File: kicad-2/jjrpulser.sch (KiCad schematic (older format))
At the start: 20 parts, among them J1 USB_OTG, J3 Screw_Terminal_HOT, J4 Screw_Terminal_COLD, J5 Conn_UART, U1 ESP-12, U2 NCP1117-3.3_SOT223

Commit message: Разводка в процессе
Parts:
- removed J1: USB_OTG, Connectors:USB_Micro-B, symbol USB_OTG
- C1: value 100mkF -> 10mkF 16v
- C2: value 470mkF -> 22mkF 5v
- U2: value NCP1117-3.3_SOT223 -> AMS1117-3.3_SOT223
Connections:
- no-connect marks 9 -> 5
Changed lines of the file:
@@
 LIBS:valves
 LIBS:ESP8266
+LIBS:jjrpulser-cache
 EELAYER 25 0
 EELAYER END
@@
 P 3450 3600
 F 0 "#FLG013" H 3450 3675 50  0001 C CNN
-F 1 "PWR_FLAG" H 3450 3750 50  0000 C CNN
+F 1 "PWR_FLAG" V 3450 3750 50  0000 L CNN
 F 2 "" H 3450 3600 50  0001 C CNN
 F 3 "" H 3450 3600 50  0001 C CNN
@@
 P 2750 3600
 F 0 "U2" H 2600 3725 50  0000 C CNN
-F 1 "NCP1117-3.3_SOT223" H 2750 3725 50  0000 L CNN
+F 1 "AMS1117-3.3_SOT223" V 2750 3725 50  0000 L CNN
 F 2 "TO_SOT_Packages_SMD:SOT-223-3Lead_TabPin2" H 2750 3800 50  0001 C CNN
 F 3 "" H 2850 3350 50  0001 C CNN
 	1    2750 3600
-	1    0    0    -1
-$EndComp
-$Comp
-L USB_OTG J1
-U 1 1 5D018B49
-P 1800 3800
-F 0 "J1" H 1600 4250 50  0000 L CNN
-F 1 "USB_OTG" H 1600 4150 50  0000 L CNN
-F 2 "Connectors:USB_Micro-B" H 1950 3750 50  0001 C CNN
-F 3 "" H 1950 3750 50  0001 C CNN
-	1    1800 3800
 	1    0    0    -1
 $EndComp
@@
 P 2300 3750
 F 0 "C1" H 2325 3850 50  0000 L CNN
-F 1 "100mkF" H 2325 3650 50  0000 L CNN
+F 1 "10mkF 16v" V 2325 3650 50  0000 R CNN
 F 2 "Capacitors_SMD:CP_Elec_6.3x5.3" H 2338 3600 50  0001 C CNN
 F 3 "" H 2300 3750 50  0001 C CNN
@@
 P 3200 3750
 F 0 "C2" H 3225 3850 50  0000 L CNN
-F 1 "470mkF" H 3225 3650 50  0000 L CNN
+F 1 "22mkF 5v" V 3225 3650 50  0000 R CNN
 F 2 "Capacitors_SMD:CP_Elec_6.3x5.3" H 3238 3600 50  0001 C CNN
 F 3 "" H 3200 3750 50  0001 C CNN
@@
 	1    0    0    -1
 $EndComp
-NoConn ~ 1700 4200
-NoConn ~ 2100 3800
-NoConn ~ 2100 3900
-NoConn ~ 2100 4000
 $Comp
 L Earth #PWR021
@@
 P 2100 3600
 F 0 "#FLG022" H 2100 3675 50  0001 C CNN
-F 1 "PWR_FLAG" H 2100 3750 50  0000 C CNN
+F 1 "PWR_FLAG" V 2100 3750 50  0000 L CNN
 F 2 "" H 2100 3600 50  0001 C CNN
 F 3 "" H 2100 3600 50  0001 C CNN

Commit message: Новая разводка: замена micro-USB на обычный разъем питания
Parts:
- added J1: Conn_Coaxial_Power, Connectors_TE-Connectivity:BNC_Socket_TYCO-AMP_LargePads, symbol Conn_Coaxial_Power
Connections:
- net +5V: now also C1.1, U2.3 (VI), J1.1 (In)
- net Earth: now also J1.2 (Ext)
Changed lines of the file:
@@
 $EndComp
 Wire Wire Line
-	2100 3600 2450 3600
+	1800 3600 2450 3600
 $Comp
 L CP C1
@@
 L Earth #PWR018
 U 1 1 5D018FC9
-P 1800 4200
-F 0 "#PWR018" H 1800 3950 50  0001 C CNN
-F 1 "Earth" H 1800 4050 50  0001 C CNN
-F 2 "" H 1800 4200 50  0001 C CNN
-F 3 "" H 1800 4200 50  0001 C CNN
-	1    1800 4200
+P 1800 3900
+F 0 "#PWR018" H 1800 3650 50  0001 C CNN
+F 1 "Earth" H 1800 3750 50  0001 C CNN
+F 2 "" H 1800 3900 50  0001 C CNN
+F 3 "" H 1800 3900 50  0001 C CNN
+	1    1800 3900
 	1    0    0    -1
 $EndComp
@@
 	1    0    0    -1
 $EndComp
+$Comp
+L Conn_Coaxial_Power J1
+U 1 1 5D07B797
+P 1800 3700
+F 0 "J1" V 1600 3650 50  0000 C CNN
+F 1 "Conn_Coaxial_Power" V 1675 3650 50  0000 C CNN
+F 2 "Connectors_TE-Connectivity:BNC_Socket_TYCO-AMP_LargePads" H 1800 3650 50  0001 C CNN
+F 3 "" H 1800 3650 50  0001 C CNN
+	1    1800 3700
+	1    0    0    -1
+$EndComp
+$Comp
+L +5V #PWR023
+U 1 1 5D07B846
+P 1800 3600
+F 0 "#PWR023" H 1800 3450 50  0001 C CNN
+F 1 "+5V" H 1800 3740 50  0000 C CNN
+F 2 "" H 1800 3600 50  0001 C CNN
+F 3 "" H 1800 3600 50  0001 C CNN
+	1    1800 3600
+	1    0    0    -1
+$EndComp
+Connection ~ 2100 3600
 $EndSCHEMATC

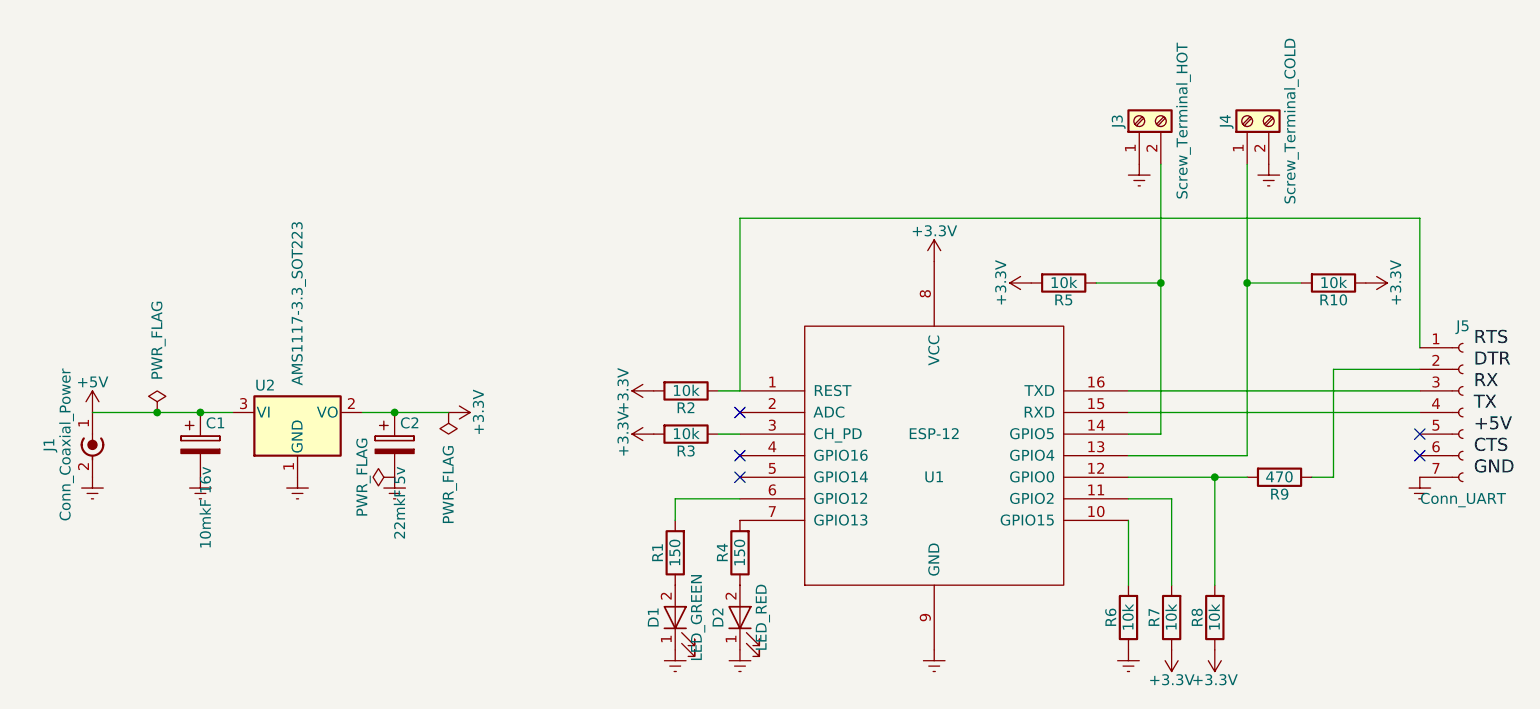
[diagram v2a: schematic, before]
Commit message: Разводка2: +5V с UART - программирование и консоль без внешнего питания. GPIO16 <--> RESET - выход из deep sleep
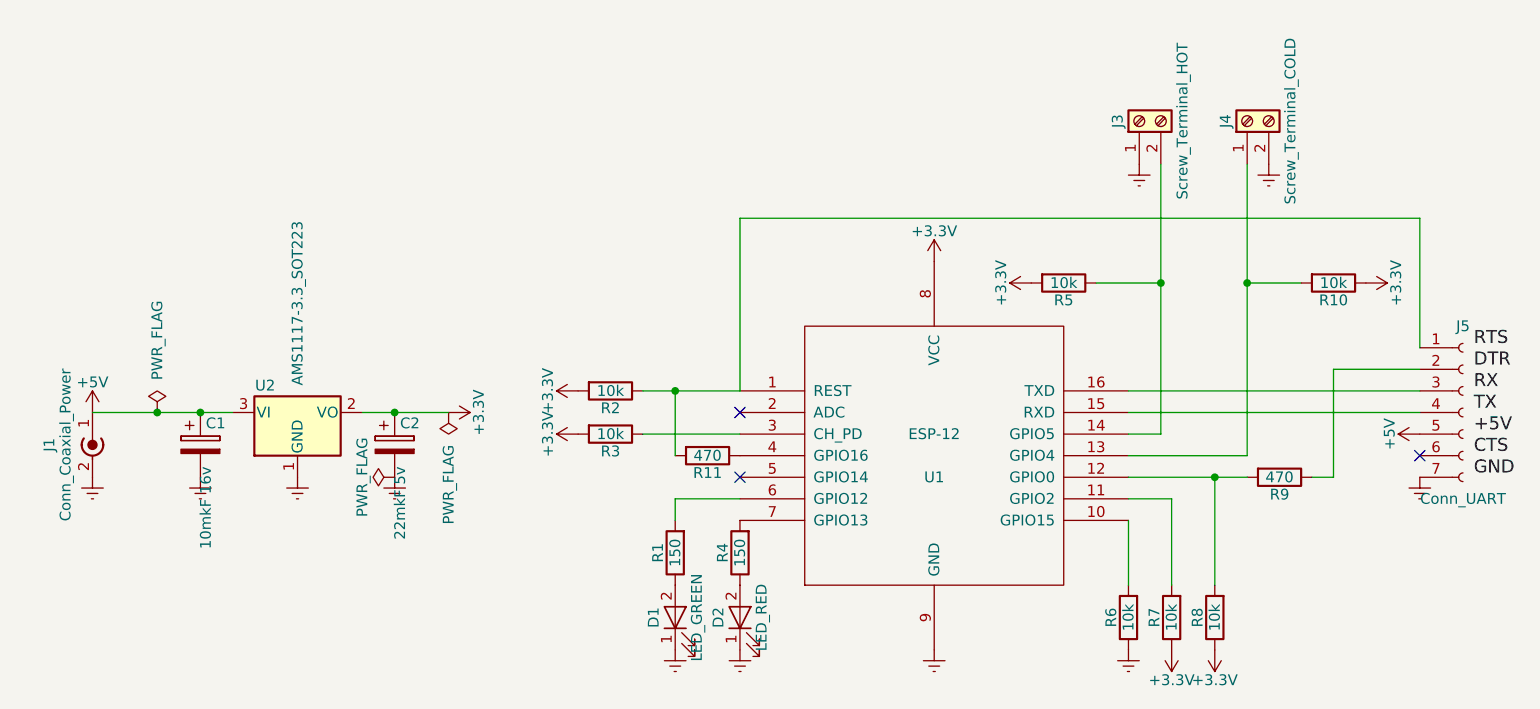
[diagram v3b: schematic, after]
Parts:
- added R11: 470, Resistors_SMD:R_0805_HandSoldering, symbol R
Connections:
- net +5V: now also J5.5 (Pin_5)
- net at J5.1 (Pin_1), R2.1, U1.1 (REST): now also R11.2
- net at U1.4 (GPIO16): now also R11.1
- no-connect marks 5 -> 3
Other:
- moved on the sheet: R2, R3
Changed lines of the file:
@@
 L R R2
 U 1 1 5C352E95
-P 4550 3500
-F 0 "R2" V 4630 3500 50  0000 C CNN
-F 1 "10k" V 4550 3500 50  0000 C CNN
-F 2 "Resistors_SMD:R_0805_HandSoldering" V 4480 3500 50  0001 C CNN
-F 3 "" H 4550 3500 50  0001 C CNN
-	1    4550 3500
+P 4200 3500
+F 0 "R2" V 4280 3500 50  0000 C CNN
+F 1 "10k" V 4200 3500 50  0000 C CNN
+F 2 "Resistors_SMD:R_0805_HandSoldering" V 4130 3500 50  0001 C CNN
+F 3 "" H 4200 3500 50  0001 C CNN
+	1    4200 3500
 	0    1    1    0
 $EndComp
@@
 L R R3
 U 1 1 5C35306E
-P 4550 3700
-F 0 "R3" V 4630 3700 50  0000 C CNN
-F 1 "10k" V 4550 3700 50  0000 C CNN
-F 2 "Resistors_SMD:R_0805_HandSoldering" V 4480 3700 50  0001 C CNN
-F 3 "" H 4550 3700 50  0001 C CNN
-	1    4550 3700
+P 4200 3700
+F 0 "R3" V 4280 3700 50  0000 C CNN
+F 1 "10k" V 4200 3700 50  0000 C CNN
+F 2 "Resistors_SMD:R_0805_HandSoldering" V 4130 3700 50  0001 C CNN
+F 3 "" H 4200 3700 50  0001 C CNN
+	1    4200 3700
 	0    1    1    0
 $EndComp
@@
 $EndComp
 $Comp
-L +3.3V #PWR01
+L +3.3V #PWR11
 U 1 1 5C353620
 P 5700 2900
-F 0 "#PWR01" H 5700 2750 50  0001 C CNN
+F 0 "#PWR11" H 5700 2750 50  0001 C CNN
 F 1 "+3.3V" H 5700 3040 50  0000 C CNN
 F 2 "" H 5700 2900 50  0001 C CNN
@@
 $EndComp
 $Comp
-L Earth #PWR02
+L Earth #PWR12
 U 1 1 5C35375C
 P 5700 4700
-F 0 "#PWR02" H 5700 4450 50  0001 C CNN
+F 0 "#PWR12" H 5700 4450 50  0001 C CNN
 F 1 "Earth" H 5700 4550 50  0001 C CNN
 F 2 "" H 5700 4700 50  0001 C CNN
@@
 $EndComp
 $Comp
-L Earth #PWR03
+L Earth #PWR14
 U 1 1 5C3547A3
 P 6600 4700
-F 0 "#PWR03" H 6600 4450 50  0001 C CNN
+F 0 "#PWR14" H 6600 4450 50  0001 C CNN
 F 1 "Earth" H 6600 4550 50  0001 C CNN
 F 2 "" H 6600 4700 50  0001 C CNN
@@
 GND
 $Comp
-L +3.3V #PWR04
+L +3.3V #PWR19
 U 1 1 5C35542B
 P 7700 3000
-F 0 "#PWR04" H 7700 2850 50  0001 C CNN
+F 0 "#PWR19" H 7700 2850 50  0001 C CNN
 F 1 "+3.3V" H 7700 3140 50  0000 C CNN
 F 2 "" H 7700 3000 50  0001 C CNN
@@
 $EndComp
 $Comp
-L +3.3V #PWR05
+L +3.3V #PWR17
 U 1 1 5C3554B7
 P 7000 4700
-F 0 "#PWR05" H 7000 4550 50  0001 C CNN
+F 0 "#PWR17" H 7000 4550 50  0001 C CNN
 F 1 "+3.3V" H 7000 4840 50  0000 C CNN
 F 2 "" H 7000 4700 50  0001 C CNN
@@
 $EndComp
 $Comp
-L +3.3V #PWR06
+L +3.3V #PWR16
 U 1 1 5C3554EC
 P 6800 4700
-F 0 "#PWR06" H 6800 4550 50  0001 C CNN
+F 0 "#PWR16" H 6800 4550 50  0001 C CNN
 F 1 "+3.3V" H 6800 4840 50  0000 C CNN
 F 2 "" H 6800 4700 50  0001 C CNN
@@
 $EndComp
 $Comp
-L Earth #PWR07
+L Earth #PWR21
 U 1 1 5C3555CB
 P 7950 3900
-F 0 "#PWR07" H 7950 3650 50  0001 C CNN
+F 0 "#PWR21" H 7950 3650 50  0001 C CNN
 F 1 "Earth" H 7950 3750 50  0001 C CNN
 F 2 "" H 7950 3900 50  0001 C CNN
@@
 $EndComp
 $Comp
-L +3.3V #PWR08
+L +3.3V #PWR13
 U 1 1 5C355706
 P 6150 3000
-F 0 "#PWR08" H 6150 2850 50  0001 C CNN
+F 0 "#PWR13" H 6150 2850 50  0001 C CNN
 F 1 "+3.3V" H 6150 3140 50  0000 C CNN
 F 2 "" H 6150 3000 50  0001 C CNN
@@
 $EndComp
 $Comp
-L Earth #PWR09
+L Earth #PWR9
 U 1 1 5C35594F
 P 4500 4700
-F 0 "#PWR09" H 4500 4450 50  0001 C CNN
+F 0 "#PWR9" H 4500 4450 50  0001 C CNN
 F 1 "Earth" H 4500 4550 50  0001 C CNN
 F 2 "" H 4500 4700 50  0001 C CNN
@@
 $EndComp
 $Comp
-L Earth #PWR010
+L Earth #PWR10
 U 1 1 5C3559DA
 P 4800 4700
-F 0 "#PWR010" H 4800 4450 50  0001 C CNN
+F 0 "#PWR10" H 4800 4450 50  0001 C CNN
 F 1 "Earth" H 4800 4550 50  0001 C CNN
 F 2 "" H 4800 4700 50  0001 C CNN
@@
 $EndComp
 NoConn ~ 4800 3900
-NoConn ~ 4800 3800
-NoConn ~ 7950 3700
 NoConn ~ 7950 3800
 NoConn ~ 4800 3600
 $Comp
-L +3.3V #PWR011
+L +3.3V #PWR7
 U 1 1 5C355B7E
-P 4400 3500
-F 0 "#PWR011" H 4400 3350 50  0001 C CNN
-F 1 "+3.3V" H 4400 3640 50  0000 C CNN
-F 2 "" H 4400 3500 50  0001 C CNN
-F 3 "" H 4400 3500 50  0001 C CNN
-	1    4400 3500
-	0    -1   -1   0
-$EndComp
-$Comp
-L +3.3V #PWR012
+P 4050 3500
+F 0 "#PWR7" H 4050 3350 50  0001 C CNN
+F 1 "+3.3V" H 4050 3640 50  0000 C CNN
+F 2 "" H 4050 3500 50  0001 C CNN
+F 3 "" H 4050 3500 50  0001 C CNN
+	1    4050 3500
+	0    -1   -1   0
+$EndComp
+$Comp
+L +3.3V #PWR8
 U 1 1 5C355C5B
-P 4400 3700
-F 0 "#PWR012" H 4400 3550 50  0001 C CNN
-F 1 "+3.3V" H 4400 3840 50  0000 C CNN
-F 2 "" H 4400 3700 50  0001 C CNN
-F 3 "" H 4400 3700 50  0001 C CNN
-	1    4400 3700
-	0    -1   -1   0
-$EndComp
-$Comp
-L PWR_FLAG #FLG013
+P 4050 3700
+F 0 "#PWR8" H 4050 3550 50  0001 C CNN
+F 1 "+3.3V" H 4050 3840 50  0000 C CNN
+F 2 "" H 4050 3700 50  0001 C CNN
+F 3 "" H 4050 3700 50  0001 C CNN
+	1    4050 3700
+	0    -1   -1   0
+$EndComp
+$Comp
+L PWR_FLAG #FLG3
 U 1 1 5C356F0A
 P 3450 3600
-F 0 "#FLG013" H 3450 3675 50  0001 C CNN
+F 0 "#FLG3" H 3450 3675 50  0001 C CNN
 F 1 "PWR_FLAG" V 3450 3750 50  0000 L CNN
 F 2 "" H 3450 3600 50  0001 C CNN
@@
 $EndComp
 $Comp
-L +3.3V #PWR014
+L +3.3V #PWR6
 U 1 1 5C359F14
 P 3450 3600
-F 0 "#PWR014" H 3450 3450 50  0001 C CNN
+F 0 "#PWR6" H 3450 3450 50  0001 C CNN
 F 1 "+3.3V" H 3450 3740 50  0000 C CNN
 F 2 "" H 3450 3600 50  0001 C CNN
@@
 $EndComp
 $Comp
-L Earth #PWR015
+L Earth #PWR18
 U 1 1 5CBC9513
 P 7250 2450
-F 0 "#PWR015" H 7250 2200 50  0001 C CNN
+F 0 "#PWR18" H 7250 2200 50  0001 C CNN
 F 1 "Earth" H 7250 2300 50  0001 C CNN
 F 2 "" H 7250 2450 50  0001 C CNN
@@
 $EndComp
 $Comp
-L Earth #PWR016
+L Earth #PWR15
 U 1 1 5CBC956E
 P 6650 2450
-F 0 "#PWR016" H 6650 2200 50  0001 C CNN
+F 0 "#PWR15" H 6650 2200 50  0001 C CNN
 F 1 "Earth" H 6650 2300 50  0001 C CNN
 F 2 "" H 6650 2450 50  0001 C CNN
@@
 	6600 3500 7950 3500
 Wire Wire Line
-	4700 3700 4800 3700
-Wire Wire Line
-	4700 3500 4800 3500
+	4350 3700 4800 3700
+Wire Wire Line
+	4350 3500 4800 3500
 Wire Wire Line
 	4800 3500 4800 2700
@@
 	6600 3900 7150 3900
 $Comp
-L PWR_FLAG #FLG017
+L PWR_FLAG #FLG2
 U 1 1 5CBE1549
 P 3200 3900
-F 0 "#FLG017" H 3200 3975 50  0001 C CNN
+F 0 "#FLG2" H 3200 3975 50  0001 C CNN
 F 1 "PWR_FLAG" H 3200 4050 50  0000 C CNN
 F 2 "" H 3200 3900 50  0001 C CNN
@@
 $EndComp
 $Comp
-L Earth #PWR018
+L Earth #PWR2
 U 1 1 5D018FC9
 P 1800 3900
-F 0 "#PWR018" H 1800 3650 50  0001 C CNN
+F 0 "#PWR2" H 1800 3650 50  0001 C CNN
 F 1 "Earth" H 1800 3750 50  0001 C CNN
 F 2 "" H 1800 3900 50  0001 C CNN
@@
 $EndComp
 $Comp
-L Earth #PWR019
+L Earth #PWR3
 U 1 1 5D0190D4
 P 2300 3900
-F 0 "#PWR019" H 2300 3650 50  0001 C CNN
+F 0 "#PWR3" H 2300 3650 50  0001 C CNN
 F 1 "Earth" H 2300 3750 50  0001 C CNN
 F 2 "" H 2300 3900 50  0001 C CNN
@@
 Connection ~ 3200 3600
 $Comp
-L Earth #PWR020
+L Earth #PWR5
 U 1 1 5D019215
 P 3200 3900
-F 0 "#PWR020" H 3200 3650 50  0001 C CNN
+F 0 "#PWR5" H 3200 3650 50  0001 C CNN
 F 1 "Earth" H 3200 3750 50  0001 C CNN
 F 2 "" H 3200 3900 50  0001 C CNN
@@
 $EndComp
 $Comp
-L Earth #PWR021
+L Earth #PWR4
 U 1 1 5D019E44
 P 2750 3900
-F 0 "#PWR021" H 2750 3650 50  0001 C CNN
+F 0 "#PWR4" H 2750 3650 50  0001 C CNN
 F 1 "Earth" H 2750 3750 50  0001 C CNN
 F 2 "" H 2750 3900 50  0001 C CNN
@@
 $EndComp
 $Comp
-L PWR_FLAG #FLG022
+L PWR_FLAG #FLG1
 U 1 1 5D01A028
 P 2100 3600
-F 0 "#FLG022" H 2100 3675 50  0001 C CNN
+F 0 "#FLG1" H 2100 3675 50  0001 C CNN
 F 1 "PWR_FLAG" V 2100 3750 50  0000 L CNN
 F 2 "" H 2100 3600 50  0001 C CNN
@@
 $EndComp
 $Comp
-L +5V #PWR023
+L +5V #PWR1
 U 1 1 5D07B846
 P 1800 3600
-F 0 "#PWR023" H 1800 3450 50  0001 C CNN
+F 0 "#PWR1" H 1800 3450 50  0001 C CNN
 F 1 "+5V" H 1800 3740 50  0000 C CNN
 F 2 "" H 1800 3600 50  0001 C CNN
@@
 $EndComp
 Connection ~ 2100 3600
+$Comp
+L +5V #PWR20
+U 1 1 5D096BA2
+P 7950 3700
+F 0 "#PWR20" H 7950 3550 50  0001 C CNN
+F 1 "+5V" H 7950 3840 50  0000 C CNN
+F 2 "" H 7950 3700 50  0001 C CNN
+F 3 "" H 7950 3700 50  0001 C CNN
+	1    7950 3700
+	0    -1   -1   0
+$EndComp
+$Comp
+L R R11
+U 1 1 5D097B09
+P 4650 3800
+F 0 "R11" V 4730 3800 50  0000 C CNN
+F 1 "470" V 4650 3800 50  0000 C CNN
+F 2 "Resistors_SMD:R_0805_HandSoldering" V 4580 3800 50  0001 C CNN
+F 3 "" H 4650 3800 50  0001 C CNN
+	1    4650 3800
+	0    1    1    0
+$EndComp
+Wire Wire Line
+	4500 3800 4500 3500
+Connection ~ 4500 3500
 $EndSCHEMATC

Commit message: Разводка2: Забытые упоминания R2010 заменены на R1206
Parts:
- R10, R5: footprint Resistors_SMD:R_2010_HandSoldering -> Resistors_SMD:R_1206_HandSoldering
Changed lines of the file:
@@
 F 0 "R5" V 6380 3000 50  0000 C CNN
 F 1 "10k" V 6300 3000 50  0000 C CNN
-F 2 "Resistors_SMD:R_2010_HandSoldering" V 6230 3000 50  0001 C CNN
+F 2 "Resistors_SMD:R_1206_HandSoldering" V 6230 3000 50  0001 C CNN
 F 3 "" H 6300 3000 50  0001 C CNN
 	1    6300 3000
@@
 F 0 "R10" V 7630 3000 50  0000 C CNN
 F 1 "10k" V 7550 3000 50  0000 C CNN
-F 2 "Resistors_SMD:R_2010_HandSoldering" V 7480 3000 50  0001 C CNN
+F 2 "Resistors_SMD:R_1206_HandSoldering" V 7480 3000 50  0001 C CNN
 F 3 "" H 7550 3000 50  0001 C CNN
 	1    7550 3000
@@
 $EndComp
 $Comp
-L +3.3V #PWR11
+L +3.3V #PWR01
 U 1 1 5C353620
 P 5700 2900
-F 0 "#PWR11" H 5700 2750 50  0001 C CNN
+F 0 "#PWR01" H 5700 2750 50  0001 C CNN
 F 1 "+3.3V" H 5700 3040 50  0000 C CNN
 F 2 "" H 5700 2900 50  0001 C CNN
@@
 $EndComp
 $Comp
-L Earth #PWR12
+L Earth #PWR02
 U 1 1 5C35375C
 P 5700 4700
-F 0 "#PWR12" H 5700 4450 50  0001 C CNN
+F 0 "#PWR02" H 5700 4450 50  0001 C CNN
 F 1 "Earth" H 5700 4550 50  0001 C CNN
 F 2 "" H 5700 4700 50  0001 C CNN
@@
 $EndComp
 $Comp
-L Earth #PWR14
+L Earth #PWR03
 U 1 1 5C3547A3
 P 6600 4700
-F 0 "#PWR14" H 6600 4450 50  0001 C CNN
+F 0 "#PWR03" H 6600 4450 50  0001 C CNN
 F 1 "Earth" H 6600 4550 50  0001 C CNN
 F 2 "" H 6600 4700 50  0001 C CNN
@@
 GND
 $Comp
-L +3.3V #PWR19
+L +3.3V #PWR04
 U 1 1 5C35542B
 P 7700 3000
-F 0 "#PWR19" H 7700 2850 50  0001 C CNN
+F 0 "#PWR04" H 7700 2850 50  0001 C CNN
 F 1 "+3.3V" H 7700 3140 50  0000 C CNN
 F 2 "" H 7700 3000 50  0001 C CNN
@@
 $EndComp
 $Comp
-L +3.3V #PWR17
+L +3.3V #PWR05
 U 1 1 5C3554B7
 P 7000 4700
-F 0 "#PWR17" H 7000 4550 50  0001 C CNN
+F 0 "#PWR05" H 7000 4550 50  0001 C CNN
 F 1 "+3.3V" H 7000 4840 50  0000 C CNN
 F 2 "" H 7000 4700 50  0001 C CNN
@@
 $EndComp
 $Comp
-L +3.3V #PWR16
+L +3.3V #PWR06
 U 1 1 5C3554EC
 P 6800 4700
-F 0 "#PWR16" H 6800 4550 50  0001 C CNN
+F 0 "#PWR06" H 6800 4550 50  0001 C CNN
 F 1 "+3.3V" H 6800 4840 50  0000 C CNN
 F 2 "" H 6800 4700 50  0001 C CNN
@@
 $EndComp
 $Comp
-L Earth #PWR21
+L Earth #PWR07
 U 1 1 5C3555CB
 P 7950 3900
-F 0 "#PWR21" H 7950 3650 50  0001 C CNN
+F 0 "#PWR07" H 7950 3650 50  0001 C CNN
 F 1 "Earth" H 7950 3750 50  0001 C CNN
 F 2 "" H 7950 3900 50  0001 C CNN
@@
 $EndComp
 $Comp
-L +3.3V #PWR13
+L +3.3V #PWR08
 U 1 1 5C355706
 P 6150 3000
-F 0 "#PWR13" H 6150 2850 50  0001 C CNN
+F 0 "#PWR08" H 6150 2850 50  0001 C CNN
 F 1 "+3.3V" H 6150 3140 50  0000 C CNN
 F 2 "" H 6150 3000 50  0001 C CNN
@@
 $EndComp
 $Comp
-L Earth #PWR9
+L Earth #PWR09
 U 1 1 5C35594F
 P 4500 4700
-F 0 "#PWR9" H 4500 4450 50  0001 C CNN
+F 0 "#PWR09" H 4500 4450 50  0001 C CNN
 F 1 "Earth" H 4500 4550 50  0001 C CNN
 F 2 "" H 4500 4700 50  0001 C CNN
@@
 $EndComp
 $Comp
-L Earth #PWR10
+L Earth #PWR010
 U 1 1 5C3559DA
 P 4800 4700
-F 0 "#PWR10" H 4800 4450 50  0001 C CNN
+F 0 "#PWR010" H 4800 4450 50  0001 C CNN
 F 1 "Earth" H 4800 4550 50  0001 C CNN
 F 2 "" H 4800 4700 50  0001 C CNN
@@
 NoConn ~ 4800 3600
 $Comp
-L +3.3V #PWR7
+L +3.3V #PWR011
 U 1 1 5C355B7E
 P 4050 3500
-F 0 "#PWR7" H 4050 3350 50  0001 C CNN
+F 0 "#PWR011" H 4050 3350 50  0001 C CNN
 F 1 "+3.3V" H 4050 3640 50  0000 C CNN
 F 2 "" H 4050 3500 50  0001 C CNN
@@
 $EndComp
 $Comp
-L +3.3V #PWR8
+L +3.3V #PWR012
 U 1 1 5C355C5B
 P 4050 3700
-F 0 "#PWR8" H 4050 3550 50  0001 C CNN
+F 0 "#PWR012" H 4050 3550 50  0001 C CNN
 F 1 "+3.3V" H 4050 3840 50  0000 C CNN
 F 2 "" H 4050 3700 50  0001 C CNN
@@
 $EndComp
 $Comp
-L PWR_FLAG #FLG3
+L PWR_FLAG #FLG013
 U 1 1 5C356F0A
 P 3450 3600
-F 0 "#FLG3" H 3450 3675 50  0001 C CNN
+F 0 "#FLG013" H 3450 3675 50  0001 C CNN
 F 1 "PWR_FLAG" V 3450 3750 50  0000 L CNN
 F 2 "" H 3450 3600 50  0001 C CNN
@@
 $EndComp
 $Comp
-L +3.3V #PWR6
+L +3.3V #PWR014
 U 1 1 5C359F14
 P 3450 3600
-F 0 "#PWR6" H 3450 3450 50  0001 C CNN
+F 0 "#PWR014" H 3450 3450 50  0001 C CNN
 F 1 "+3.3V" H 3450 3740 50  0000 C CNN
 F 2 "" H 3450 3600 50  0001 C CNN
@@
 $EndComp
 $Comp
-L Earth #PWR18
+L Earth #PWR015
 U 1 1 5CBC9513
 P 7250 2450
-F 0 "#PWR18" H 7250 2200 50  0001 C CNN
+F 0 "#PWR015" H 7250 2200 50  0001 C CNN
 F 1 "Earth" H 7250 2300 50  0001 C CNN
 F 2 "" H 7250 2450 50  0001 C CNN
@@
 $EndComp
 $Comp
-L Earth #PWR15
+L Earth #PWR016
 U 1 1 5CBC956E
 P 6650 2450
-F 0 "#PWR15" H 6650 2200 50  0001 C CNN
+F 0 "#PWR016" H 6650 2200 50  0001 C CNN
 F 1 "Earth" H 6650 2300 50  0001 C CNN
 F 2 "" H 6650 2450 50  0001 C CNN
@@
 	6600 3900 7150 3900
 $Comp
-L PWR_FLAG #FLG2
+L PWR_FLAG #FLG017
 U 1 1 5CBE1549
 P 3200 3900
-F 0 "#FLG2" H 3200 3975 50  0001 C CNN
+F 0 "#FLG017" H 3200 3975 50  0001 C CNN
 F 1 "PWR_FLAG" H 3200 4050 50  0000 C CNN
 F 2 "" H 3200 3900 50  0001 C CNN
@@
 $EndComp
 $Comp
-L Earth #PWR2
+L Earth #PWR018
 U 1 1 5D018FC9
 P 1800 3900
-F 0 "#PWR2" H 1800 3650 50  0001 C CNN
+F 0 "#PWR018" H 1800 3650 50  0001 C CNN
 F 1 "Earth" H 1800 3750 50  0001 C CNN
 F 2 "" H 1800 3900 50  0001 C CNN
@@
 $EndComp
 $Comp
-L Earth #PWR3
+L Earth #PWR019
 U 1 1 5D0190D4
 P 2300 3900
-F 0 "#PWR3" H 2300 3650 50  0001 C CNN
+F 0 "#PWR019" H 2300 3650 50  0001 C CNN
 F 1 "Earth" H 2300 3750 50  0001 C CNN
 F 2 "" H 2300 3900 50  0001 C CNN
@@
 Connection ~ 3200 3600
 $Comp
-L Earth #PWR5
+L Earth #PWR020
 U 1 1 5D019215
 P 3200 3900
-F 0 "#PWR5" H 3200 3650 50  0001 C CNN
+F 0 "#PWR020" H 3200 3650 50  0001 C CNN
 F 1 "Earth" H 3200 3750 50  0001 C CNN
 F 2 "" H 3200 3900 50  0001 C CNN
@@
 $EndComp
 $Comp
-L Earth #PWR4
+L Earth #PWR021
 U 1 1 5D019E44
 P 2750 3900
-F 0 "#PWR4" H 2750 3650 50  0001 C CNN
+F 0 "#PWR021" H 2750 3650 50  0001 C CNN
 F 1 "Earth" H 2750 3750 50  0001 C CNN
 F 2 "" H 2750 3900 50  0001 C CNN
@@
 $EndComp
 $Comp
-L PWR_FLAG #FLG1
+L PWR_FLAG #FLG022
 U 1 1 5D01A028
 P 2100 3600
-F 0 "#FLG1" H 2100 3675 50  0001 C CNN
+F 0 "#FLG022" H 2100 3675 50  0001 C CNN
 F 1 "PWR_FLAG" V 2100 3750 50  0000 L CNN
 F 2 "" H 2100 3600 50  0001 C CNN
@@
 $EndComp
 $Comp
-L +5V #PWR1
+L +5V #PWR023
 U 1 1 5D07B846
 P 1800 3600
-F 0 "#PWR1" H 1800 3450 50  0001 C CNN
+F 0 "#PWR023" H 1800 3450 50  0001 C CNN
 F 1 "+5V" H 1800 3740 50  0000 C CNN
 F 2 "" H 1800 3600 50  0001 C CNN
@@
 Connection ~ 2100 3600
 $Comp
-L +5V #PWR20
+L +5V #PWR024
 U 1 1 5D096BA2
 P 7950 3700
-F 0 "#PWR20" H 7950 3550 50  0001 C CNN
+F 0 "#PWR024" H 7950 3550 50  0001 C CNN
 F 1 "+5V" H 7950 3840 50  0000 C CNN
 F 2 "" H 7950 3700 50  0001 C CNN
